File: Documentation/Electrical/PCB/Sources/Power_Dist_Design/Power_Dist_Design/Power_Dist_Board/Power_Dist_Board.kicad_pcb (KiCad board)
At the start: 2 copper layers, 140 x 85 mm, 25 parts, among them J1 Battery Connector, J2 5V Connector, J3 3.3V Connector, U1 TPS565201, U2 TPS565201

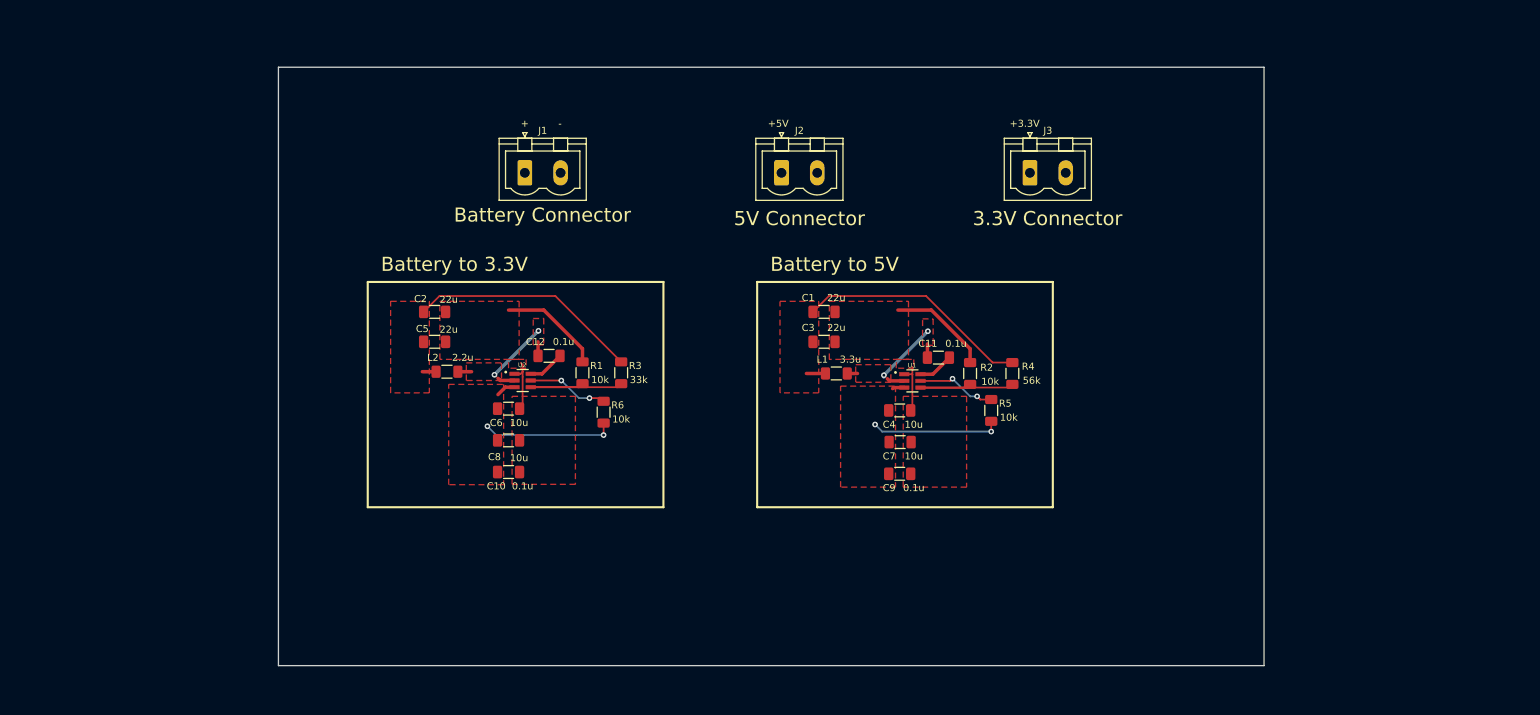
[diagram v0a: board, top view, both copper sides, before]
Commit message: Added fuses to pcb
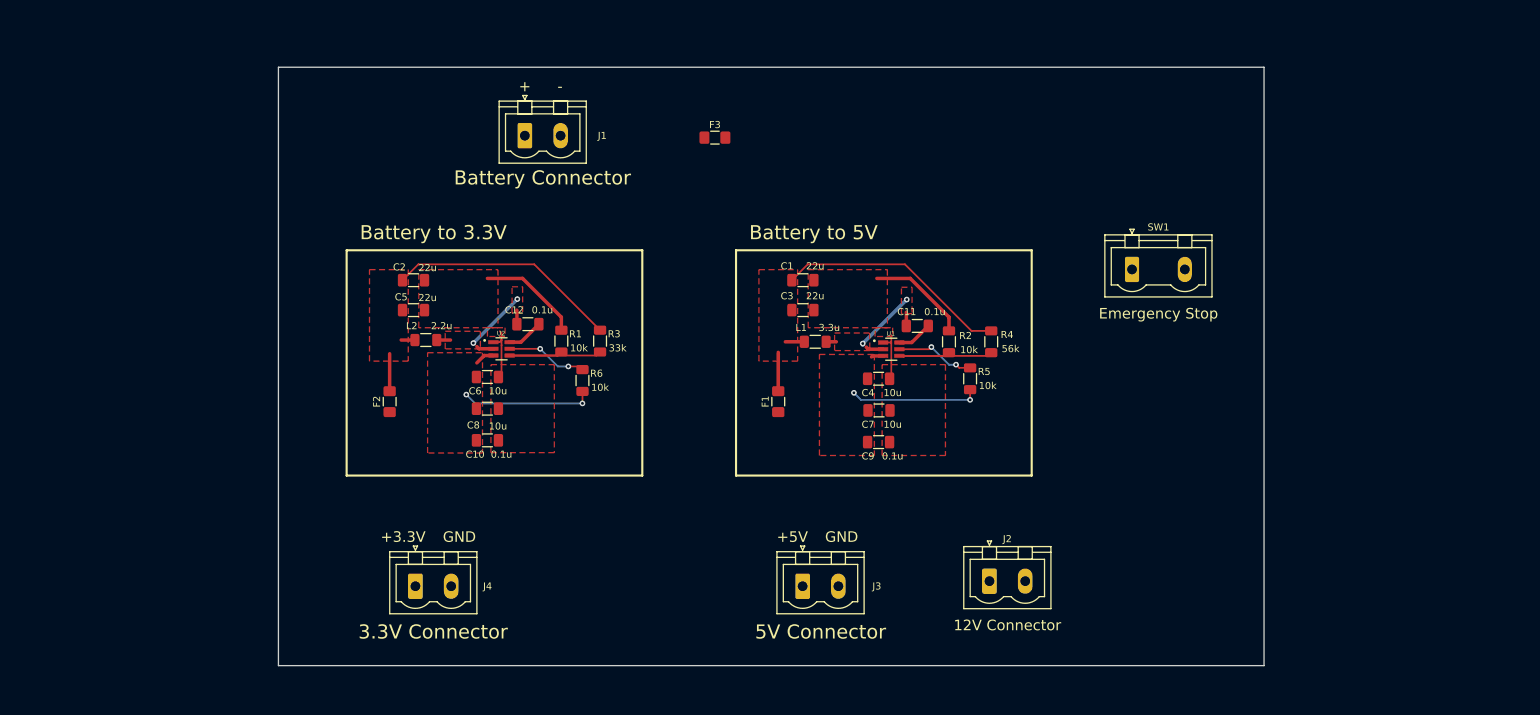
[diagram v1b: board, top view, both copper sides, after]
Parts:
- added F1: Fuse, Fuse:Fuse_1206_3216Metric_Pad1.42x1.75mm_HandSolder, F.Cu at (176.0, 72.5)
- added F2: Fuse, Fuse:Fuse_1206_3216Metric_Pad1.42x1.75mm_HandSolder, F.Cu at (120.8, 72.5)
- added F3: Fuse, Fuse:Fuse_1206_3216Metric_Pad1.42x1.75mm_HandSolder, F.Cu at (167.0, 35.0)
- added J2: 12V Connector, Connector_Phoenix_MSTB:PhoenixContact_MSTBVA_2,5_2-G-5,08_1x02_P5.08mm_Vertical, F.Cu at (206.0, 98.0)
- added SW1: Emergency Stop, Connector_Phoenix_GMSTB:PhoenixContact_GMSTBVA_2,5_2-G_1x02_P7.50mm_Vertical, F.Cu at (226.2, 53.7)
- moved J4 105.2 mm to (124.5, 98.7)
- moved J3 58.8 mm to (179.5, 98.7)
- moved R1 5.41 mm to (145.2, 63.9)
- moved R3 5.41 mm to (150.7, 63.9)
- moved C1 5.41 mm to (179.5, 55.2)
- moved C10 5.41 mm to (134.7, 78.0)
- moved C11 5.41 mm to (195.8, 61.8)
- moved C12 5.41 mm to (140.4, 61.5)
- moved C2 5.41 mm to (124.2, 55.2)
- moved C3 5.41 mm to (179.5, 59.5)
- moved C4 5.41 mm to (190.2, 69.2)
- moved C5 5.41 mm to (124.2, 59.5)
- moved C6 5.41 mm to (134.7, 69.0)
- moved C7 5.41 mm to (190.3, 73.8)
- moved C8 5.41 mm to (134.7, 73.5)
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- renumbered J2 to J3, J3 to J4
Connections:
- C1 pad 1: +5V -> /vout1
- C2 pad 1: +3.3V -> /vout2
- C3 pad 1: +5V -> /vout1
- C5 pad 1: +3.3V -> /vout2
- L1 pad 1: +5V -> /vout1
- L2 pad 1: +3.3V -> /vout2
- R3 pad 2: +3.3V -> /vout2
- R4 pad 2: +5V -> /vout1
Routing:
- net /vout1: track 0.00 -> 41.4 mm
- net /vout2: track 0.00 -> 40.1 mm
- net +5V: track 35.9 -> 0.00 mm
- net +3.3V: track 34.8 -> 0.00 mm
- added copper zone on F.Cu, net /vout1
- added copper zone on F.Cu, net /vout2
- removed copper zone on F.Cu, net +3.3V
- removed copper zone on F.Cu, net +5V
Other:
- board text added: "GND"

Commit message: Added to distribution board
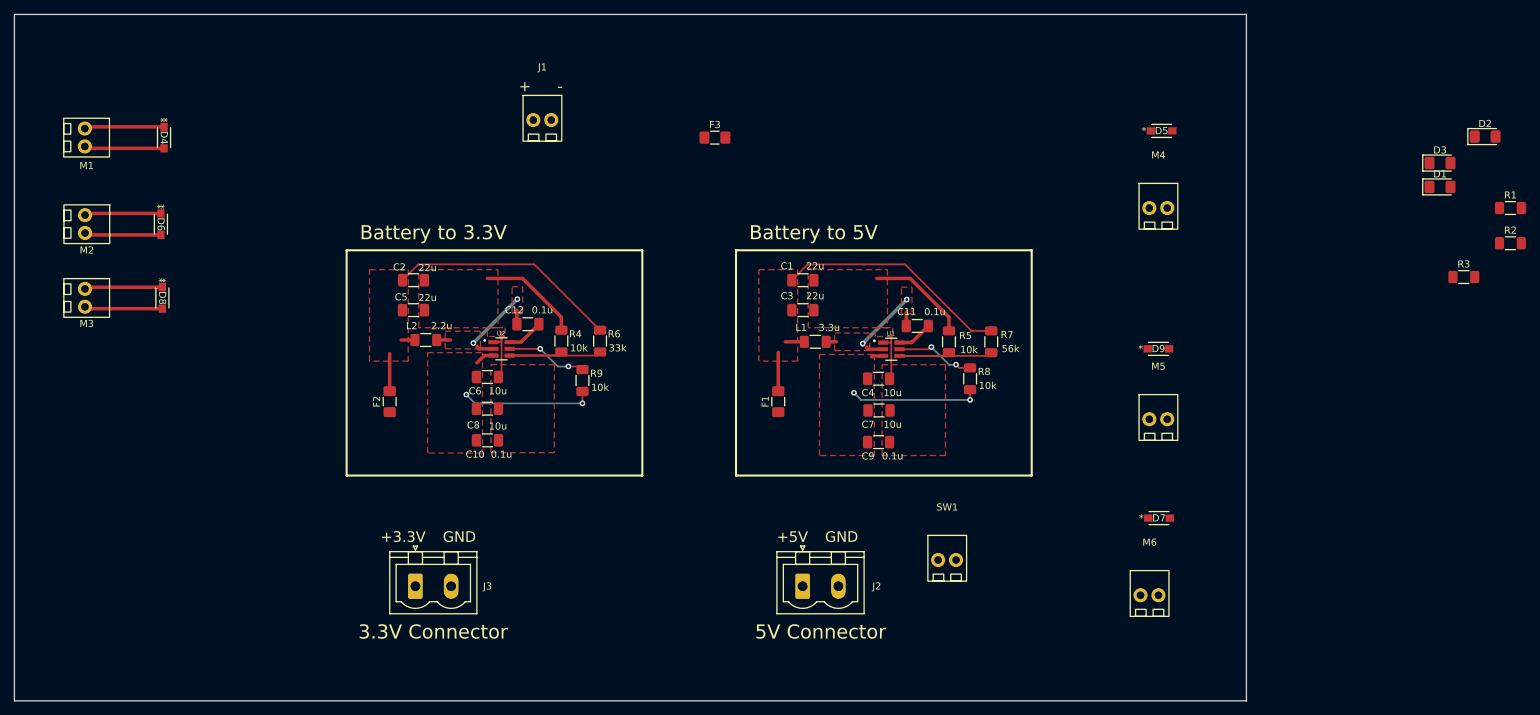
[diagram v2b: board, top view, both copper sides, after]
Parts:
- removed the J2 at (206.0, 98.0)
- added D1: LED, LED_SMD:LED_1206_3216Metric_Pad1.42x1.75mm_HandSolder, F.Cu at (270.0, 42.0)
- added D2: LED, LED_SMD:LED_1206_3216Metric_Pad1.42x1.75mm_HandSolder, F.Cu at (276.4, 34.9)
- added D3: LED, LED_SMD:LED_1206_3216Metric_Pad1.42x1.75mm_HandSolder, F.Cu at (270.0, 38.6)
- added D4: D, RB070MM:DIO_RB051MM_ROM-M, F.Cu at (88.8, 35.0)
- added D5: D, RB070MM:DIO_RB051MM_ROM-M, F.Cu at (230.4, 34.0)
- added D6: D, RB070MM:DIO_RB051MM_ROM-M, F.Cu at (88.3, 47.3)
- added D7: D, RB070MM:DIO_RB051MM_ROM-M, F.Cu at (230.1, 89.0)
- added D8: D, RB070MM:DIO_RB051MM_ROM-M, F.Cu at (88.5, 57.8)
- added D9: D, RB070MM:DIO_RB051MM_ROM-M, F.Cu at (230.0, 65.0)
- added M1: Motor_DC, Power_Dist:Molex_Screw_Term_0397730002, F.Cu at (77.5, 35.0)
- added M2: Motor_DC, Power_Dist:Molex_Screw_Term_0397730002, F.Cu at (77.5, 47.3)
- added M3: Motor_DC, Power_Dist:Molex_Screw_Term_0397730002, F.Cu at (77.5, 57.8)
- added M4: Motor_DC, Power_Dist:Molex_Screw_Term_0397730002, F.Cu at (230.0, 45.0)
- added M5: Motor_DC, Power_Dist:Molex_Screw_Term_0397730002, F.Cu at (230.0, 75.0)
- added M6: Motor_DC, Power_Dist:Molex_Screw_Term_0397730002, F.Cu at (228.8, 100.0)
- added R1: 10k, Resistor_SMD:R_1206_3216Metric_Pad1.30x1.75mm_HandSolder, F.Cu at (280.0, 45.0)
- added R2: 10k, Resistor_SMD:R_1206_3216Metric_Pad1.30x1.75mm_HandSolder, F.Cu at (280.0, 50.0)
- added R3: 10k, Resistor_SMD:R_1206_3216Metric_Pad1.30x1.75mm_HandSolder, F.Cu at (273.4, 54.8)
- J1: footprint Connector_Phoenix_MSTB:PhoenixContact_MSTBVA_2,5_2-G-5,08_1x02_P5.08mm_Vertical -> Power_Dist:Molex_Screw_Term_0397730002
- SW1: footprint Connector_Phoenix_GMSTB:PhoenixContact_GMSTBVA_2,5_2-G_1x02_P7.50mm_Vertical -> Power_Dist:Molex_Screw_Term_0397730002
- moved SW1 48.9 mm to (200.0, 95.0)
- moved J1 3.35 mm to (142.5, 32.5)
- renumbered J3 to J2, J4 to J3, R1 to R4, R2 to R5, R3 to R6, R4 to R7, R5 to R8, R6 to R9
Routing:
- net GND: track 44.4 -> 77.8 mm
- net +12V: track 0.00 -> 33.3 mm
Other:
- board size 140 x 85 mm -> 175 x 97.5 mm

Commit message: Added to power distribution pcb layout
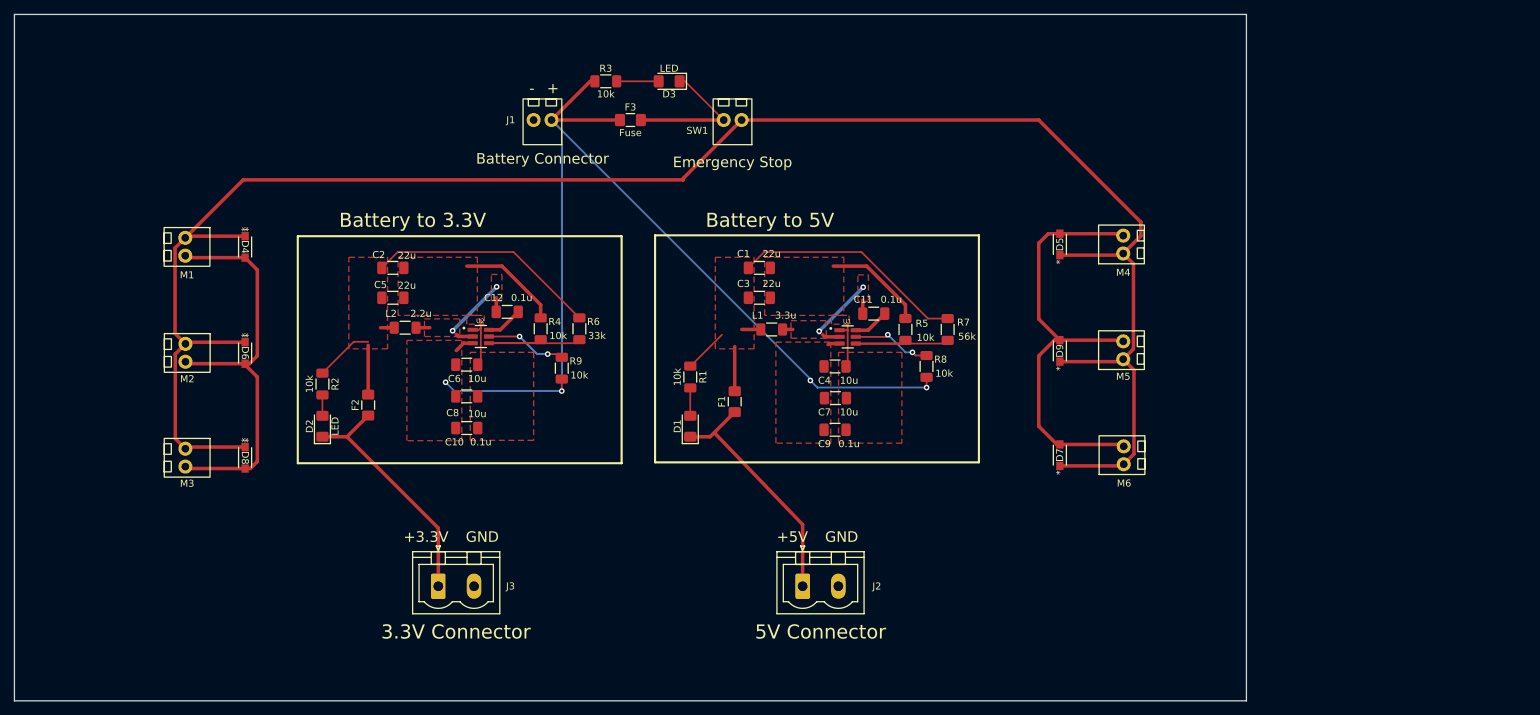
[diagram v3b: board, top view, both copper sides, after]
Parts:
- moved D2 170.2 mm to (111.2, 76.0), turned to 90 degrees
- moved R2 169.9 mm to (111.2, 70.0), turned to -90 degrees
- moved R3 125.0 mm to (151.5, 27.0)
- moved R1 118.9 mm to (163.5, 69.0), turned to -90 degrees
- moved D1 111.8 mm to (163.5, 76.0), turned to 90 degrees
- moved D3 110.1 mm to (160.5, 27.0), turned to 180 degrees
- moved SW1 69.5 mm to (169.5, 32.5), turned to 180 degrees
- moved M3 26.8 mm to (91.8, 80.5)
- moved D8 25.6 mm to (100.3, 80.5)
- moved M2 23.2 mm to (91.8, 65.6)
- moved D6 21.9 mm to (100.3, 65.6)
- moved D5 21.7 mm to (216.0, 50.2), turned to 90 degrees
- moved M1 21.1 mm to (91.8, 50.5)
- moved M6 20.2 mm to (225.1, 80.1), turned to 90 degrees
- moved D4 19.3 mm to (100.3, 50.5)
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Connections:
- SW1 pad 1: Net-(D3-Pad1) -> +12V
- SW1 pad 2: +12V -> Net-(D3-Pad1)
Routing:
- net +12V: track 33.3 -> 272.2 mm
- net /vin: track 41.6 -> 151.1 mm
- net GND: track 77.8 -> 167.8 mm
- net +5V: track 0.00 -> 34.5 mm
- net +3.3V: track 0.00 -> 34.4 mm
- net Net-(D3-Pad1): track 0.00 -> 20.3 mm
- net /vout2: track 40.1 -> 50.2 mm
- net /vout1: track 41.4 -> 48.5 mm
- net Net-(D3-Pad2): track 0.00 -> 5.96 mm
- net Net-(D1-Pad2): track 0.00 -> 3.96 mm
- net Net-(D2-Pad2): track 0.00 -> 2.96 mm
